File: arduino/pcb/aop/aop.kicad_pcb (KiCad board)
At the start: 2 copper layers, 45 x 54.5 mm, 42 parts, among them J1 Conn_01x02_Pin, M1 RFID-RC522, Q1 AO4435, SW1 SW_Push, SW2 SW_Push

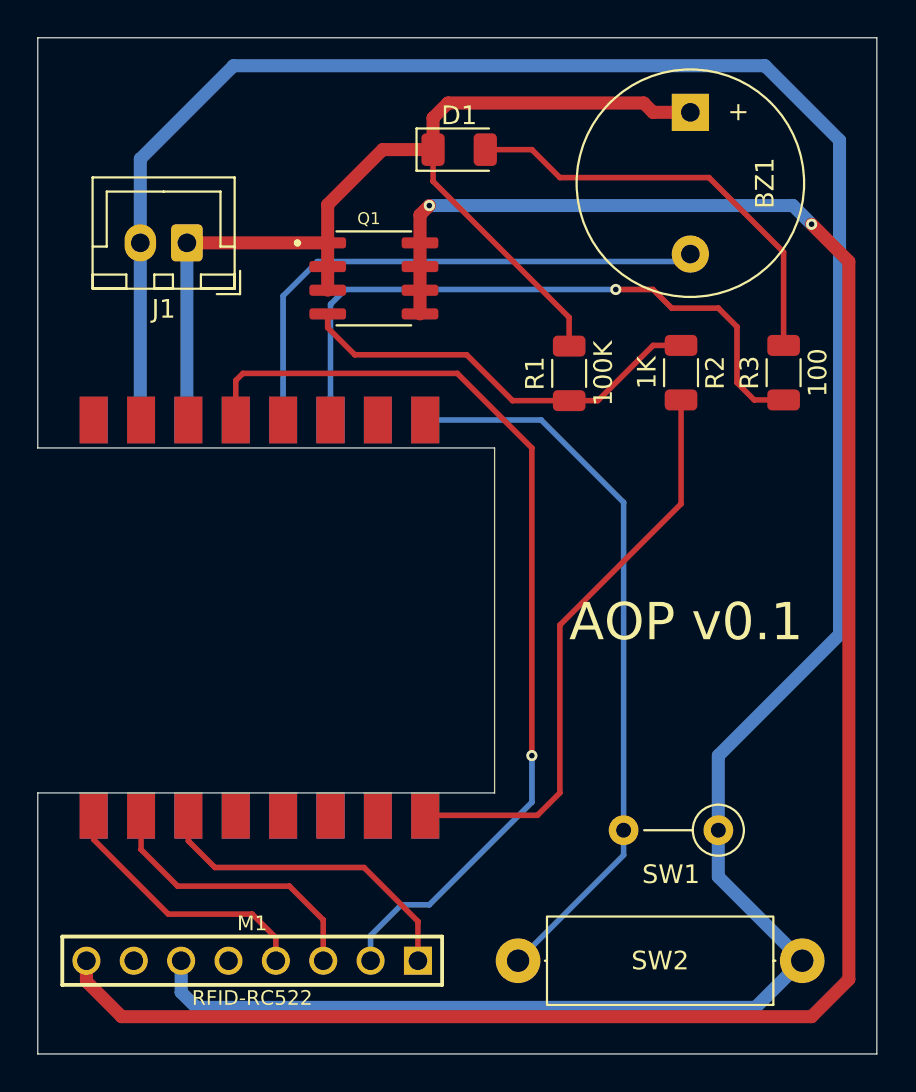
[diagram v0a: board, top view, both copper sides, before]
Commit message: [pcb] Restore through-hole esp32-c3
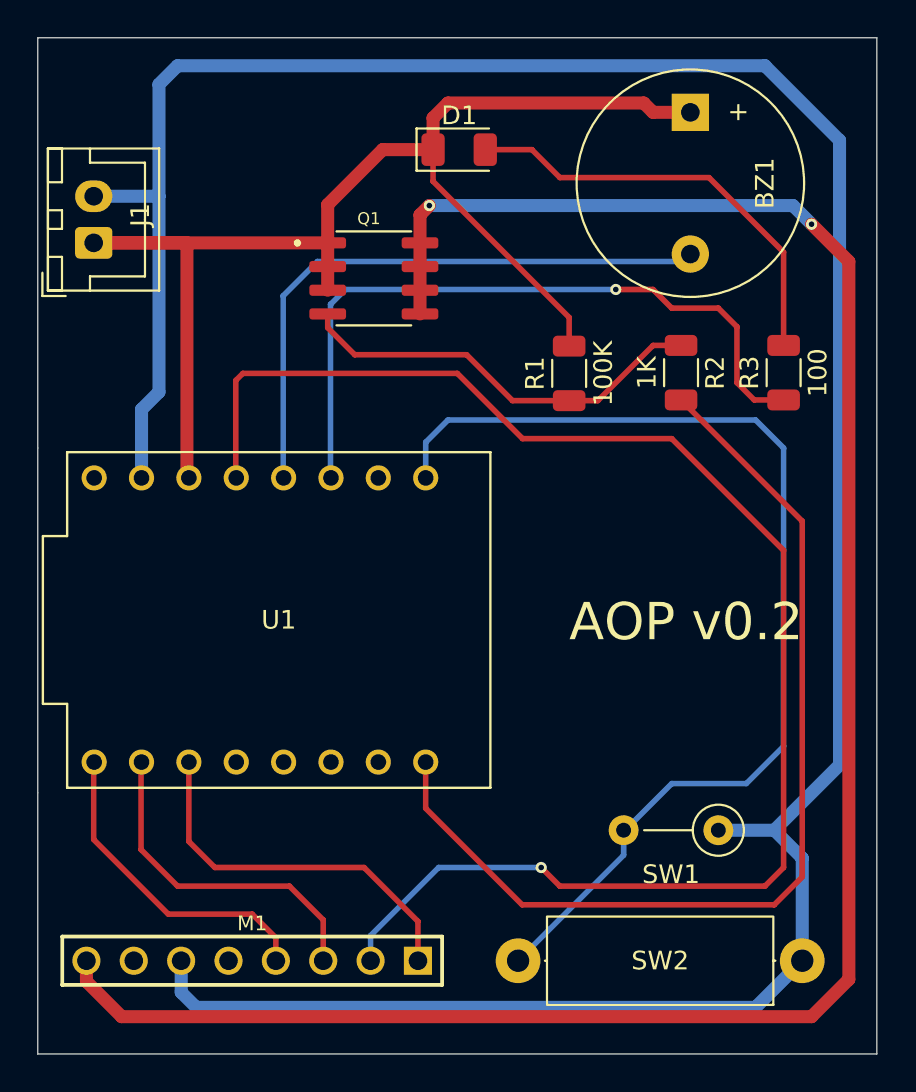
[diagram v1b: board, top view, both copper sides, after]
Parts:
- removed ? (x32): , 
- added U1: ESP32-C3_SUPERMINI_TH, ESP32-C3_SUPERMINI_TH:MODULE_ESP32-C3_SUPERMINI_TH, F.Cu at (82.4, 104.7)
- M1: value RFID-RC522 -> ~
- moved J1 5.00 mm to (72.5, 84.5), turned to 90 degrees
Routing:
- net Net-(M1-SCK): track 51.8 -> 81.5 mm
- net Net-(U1-GPIO21): track 31.5 -> 53.7 mm
- net Net-(U1-GPIO0): track 39.4 -> 58.0 mm
- net +BATT: track 58.1 -> 71.3 mm
- net GND: track 140.2 -> 149.0 mm
- net Net-(BZ1--): track 29.4 -> 32.5 mm
- net Net-(U1-GPIO2): track 35.0 -> 38.2 mm
- net Net-(M1-MISO): track 14.5 -> 17.3 mm
- net Net-(M1-MOSI): track 15.4 -> 18.2 mm
- net Net-(M1-SDA): track 17.6 -> 20.4 mm
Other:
- outline, holes or cut-outs redrawn
- board text added: "AOP v0.2"
- board text removed: "AOP v0.1"

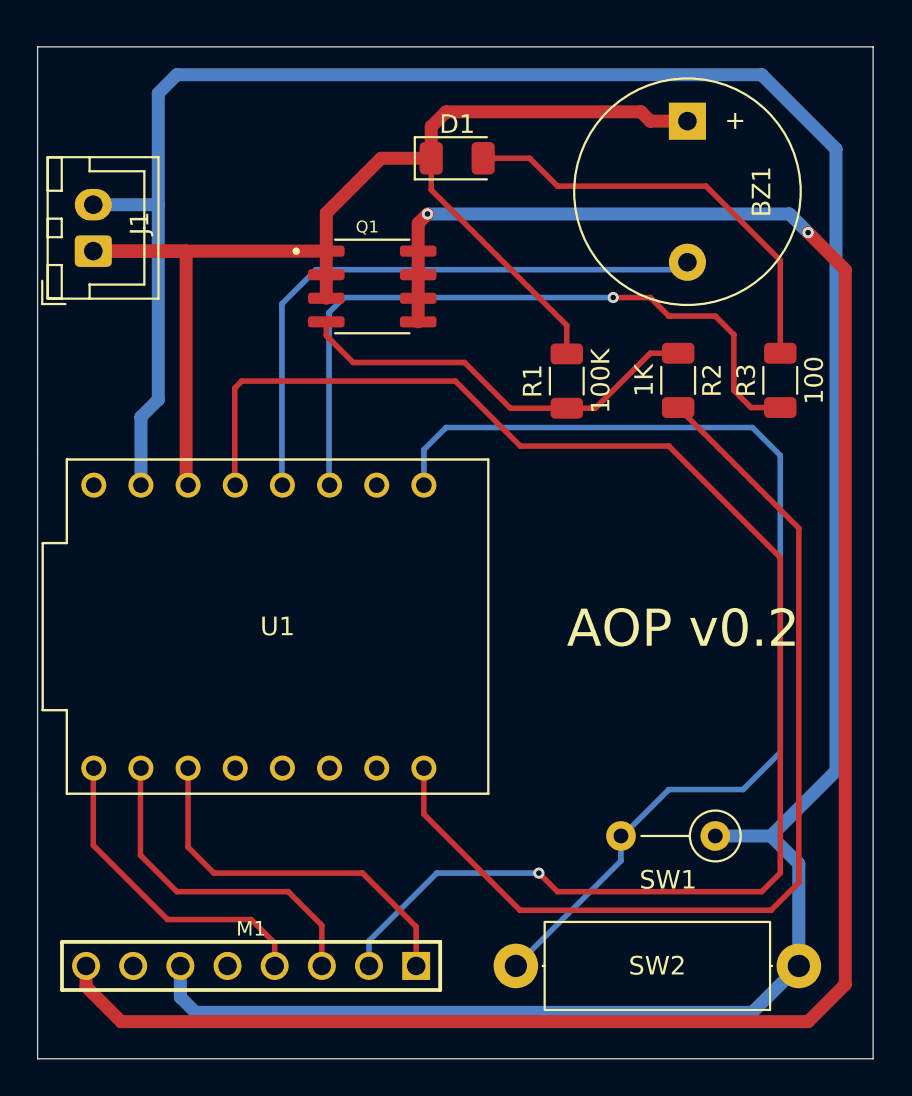
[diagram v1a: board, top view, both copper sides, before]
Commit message: [pcb] Increase the length
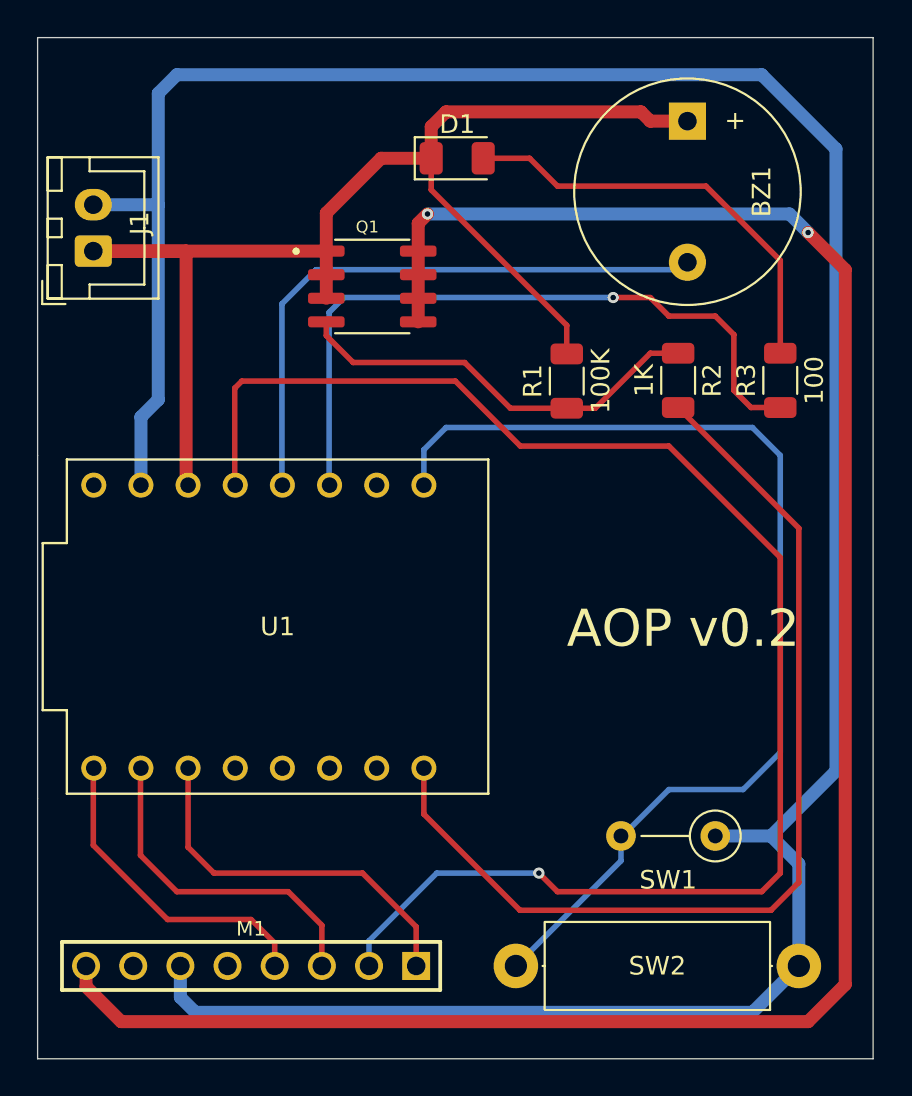
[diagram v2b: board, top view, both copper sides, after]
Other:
- board size 45 x 54.5 mm -> 45 x 55 mm
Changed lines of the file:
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@@
 			)
 		)
-		(attr through_hole)
+		(attr through_hole dnp)
 		(duplicate_pad_numbers_are_jumpers no)
 		(fp_line
@@
 	)
 	(gr_line
-		(start 69.5 73.5)
-		(end 114.5 73.5)
+		(start 69.5 73)
+		(end 114.5 73)
 		(stroke
 			(width 0.05)
@@
 	(gr_line
 		(start 69.5 95.5)
-		(end 69.5 73.5)
+		(end 69.5 73)
 		(stroke
 			(width 0.05)
@@
 	)
 	(gr_line
-		(start 114.5 73.5)
+		(start 114.5 73)
 		(end 114.5 128)
 		(stroke

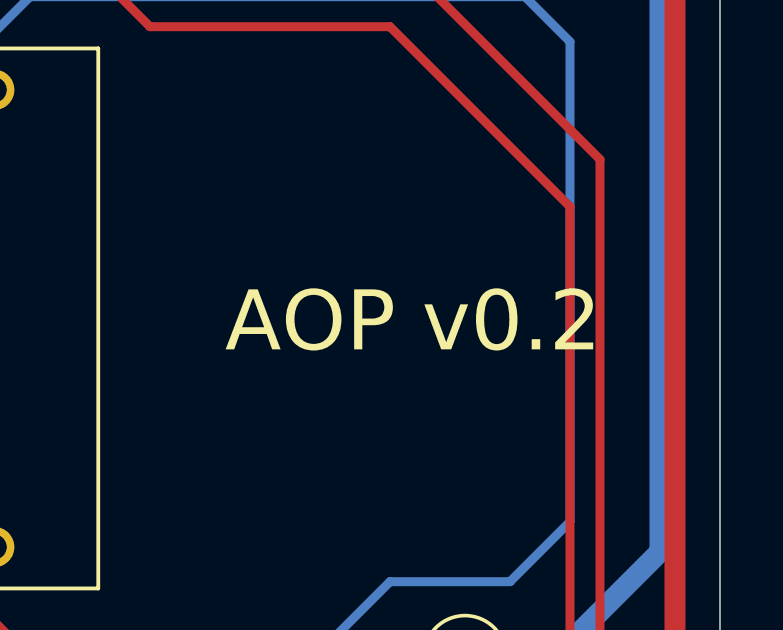
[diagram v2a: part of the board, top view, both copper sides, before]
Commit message: [pcb] Prepare 0.2 for fabrication
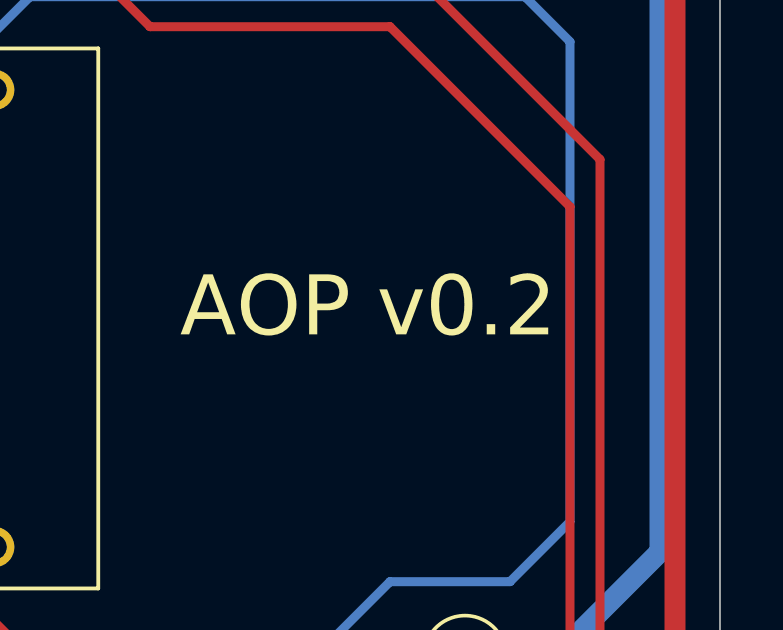
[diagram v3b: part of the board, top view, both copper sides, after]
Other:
- board text added: "${TITLE} ${REVISION}"
- board text removed: "AOP v0.2"
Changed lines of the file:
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@@
 	)
 	(paper "A4")
+	(title_block
+		(title "AOP")
+		(rev "v0.2")
+	)
 	(layers
 		(0 "F.Cu" signal)
@@
 			(drillshape 0)
 			(scaleselection 1)
-			(outputdirectory "/home/sakhnik/work/orienteering/arduin-o-punch/arduino/pcb/aop/0_1/")
+			(outputdirectory "/home/sakhnik/work/orienteering/arduin-o-punch/arduino/pcb/aop/0_2/")
 		)
 	)
@@
 		(layer "Edge.Cuts")
 	)
-	(gr_text "AOP v0.2"
-		(at 98 106 0)
+	(gr_text "${TITLE} ${REVISION}"
+		(at 96.5 105.5 0)
 		(layer "F.SilkS")
 		(effects

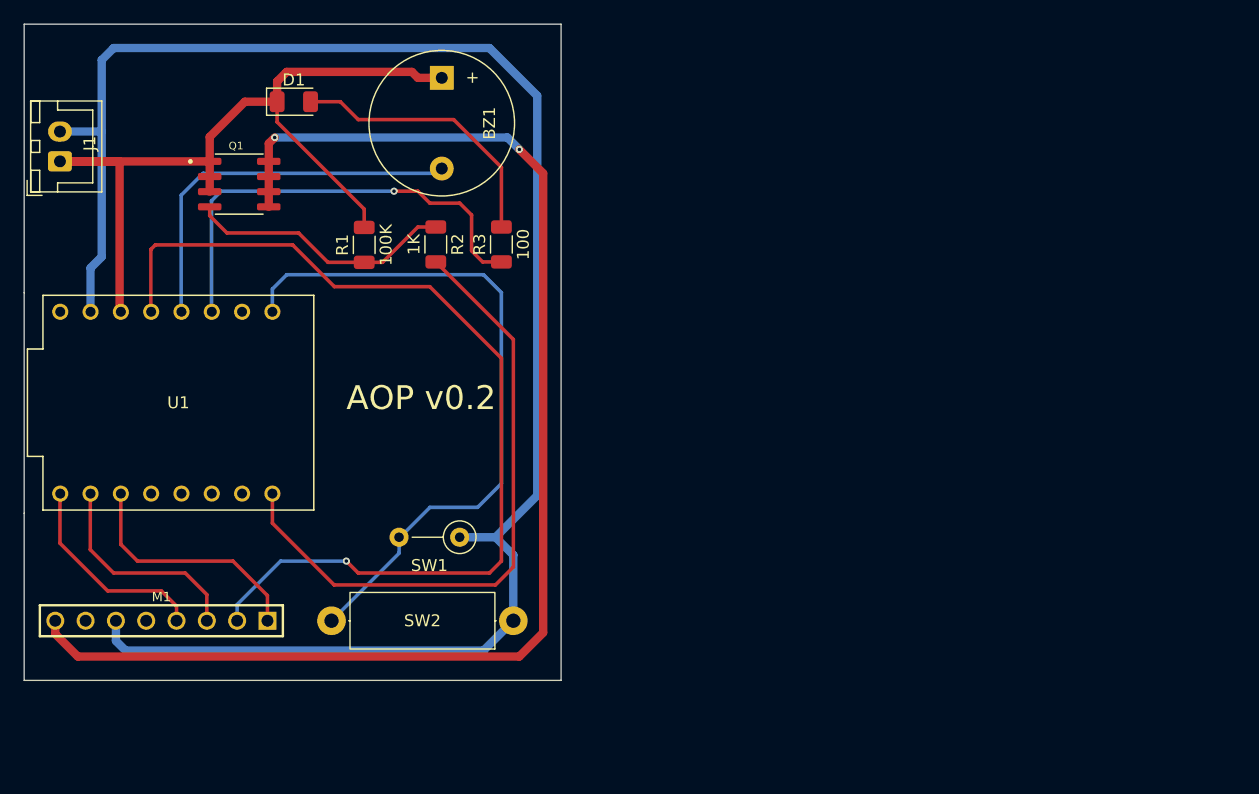
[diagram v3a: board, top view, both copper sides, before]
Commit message: [pcb] Stabilize power rail with capacitors
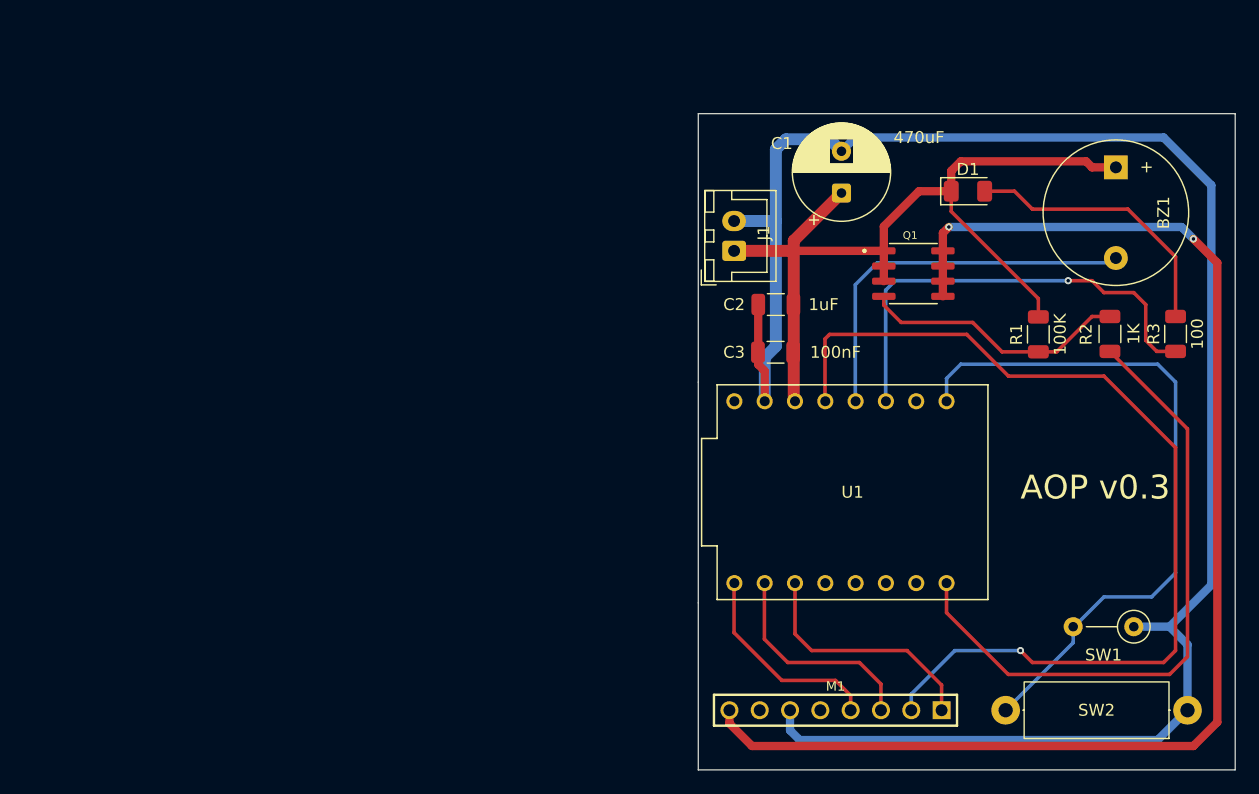
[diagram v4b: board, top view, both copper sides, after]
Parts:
- added C1: 470uF, Capacitor_THT:CP_Radial_D8.0mm_P3.50mm, F.Cu at (138.0, 87.2)
- added C2: 1uF, Capacitor_SMD:C_1206_3216Metric, F.Cu at (132.5, 96.5)
- added C3: 100nF, Capacitor_SMD:C_1206_3216Metric, F.Cu at (132.5, 100.5)
- moved U1 57.0 mm to (138.9, 112.2)
- moved BZ1 57.0 mm to (161.0, 85.0)
- moved D1 57.0 mm to (148.6, 87.0)
- moved J1 57.0 mm to (129.0, 92.0)
- moved M1 57.0 mm to (137.5, 130.5)
- moved Q1 57.0 mm to (144.0, 93.9)
- moved R1 57.0 mm to (154.5, 99.0)
- moved R2 57.0 mm to (160.5, 99.0)
- moved R3 57.0 mm to (166.0, 99.0)
- moved SW1 57.0 mm to (162.5, 123.5)
- moved SW2 57.0 mm to (167.0, 130.5)
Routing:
- net GND: track 149.0 -> 158.2 mm
- net +BATT: track 71.3 -> 72.8 mm
